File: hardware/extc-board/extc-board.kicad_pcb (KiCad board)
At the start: 2 copper layers, 38.5 x 85 mm, 19 parts, among them J1 GH BM07B link to INT, J2 VCC DATA GND, J3 PTSM 0,5/2-HH-2,5-SMD 24 VAC, J4 PTSM 0,5/2-HV-2,5-SMD 5V OUT, U1 DS2482-100, U3 TMR 12-4811WI

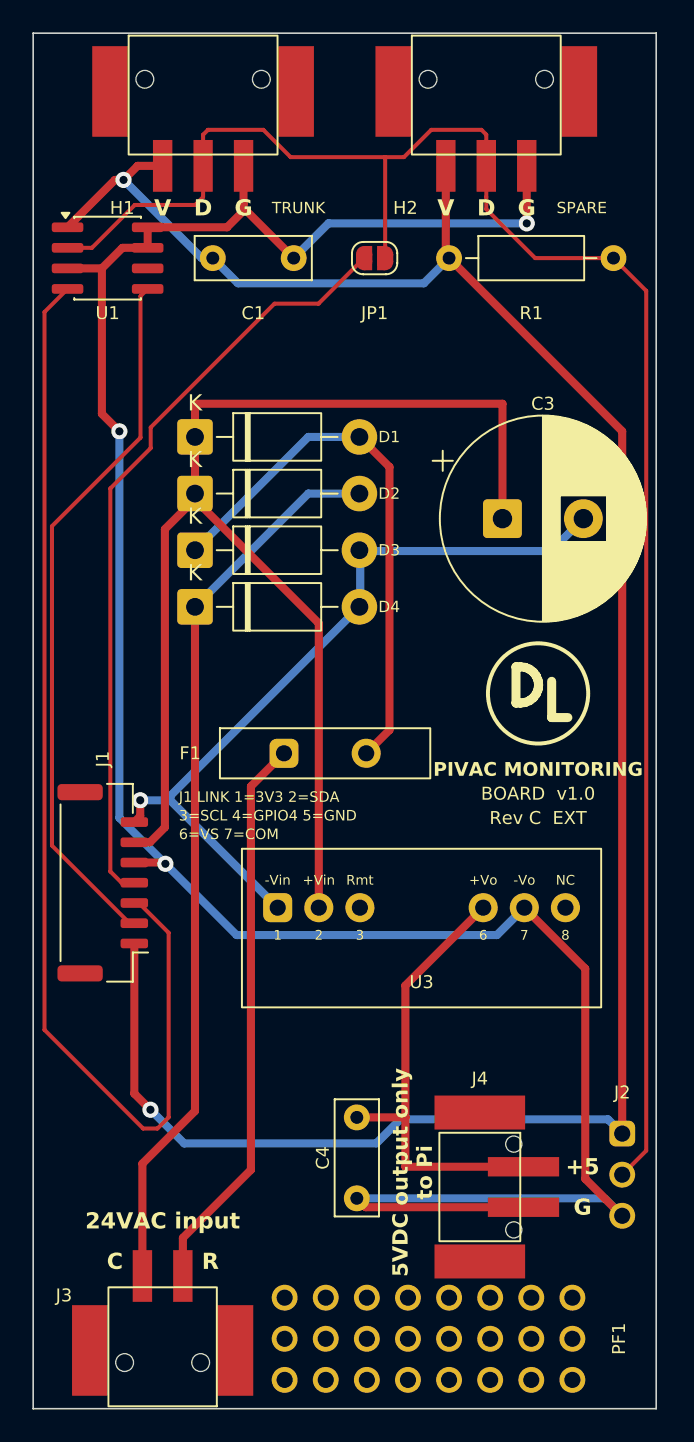
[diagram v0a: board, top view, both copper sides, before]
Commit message: Rev C: no copper under U3 but its pin escapes, no via under a legend, J1 label clear
Traco's datasheet says to avoid routing traces under the converter, whose
case is copper. The first routed board had 65 mm of track under it. Rule
areas now close the component side under the whole body and the solder
side except a 2 mm channel from each connected pin to the nearer edge,
3.5 mm away. The pins stand inside the outline, so those four escapes are
the least copper that can reach them.

The router then took the Pi's 5 V round the converter's left end, 62 mm
at 0.5 mm. It is laid by hand instead on the solder side at 1.0 mm round
the right end: 47 and 55 mm, about 25 mohm each.

Rule areas over each legend keep vias out from under the letters, which
removes the via under H2's G. The J1 reference reads left to right above
the header, clear of its mounting pad.

Co-Authored-By: Claude Fable 5.1 <noreply@anthropic.com>
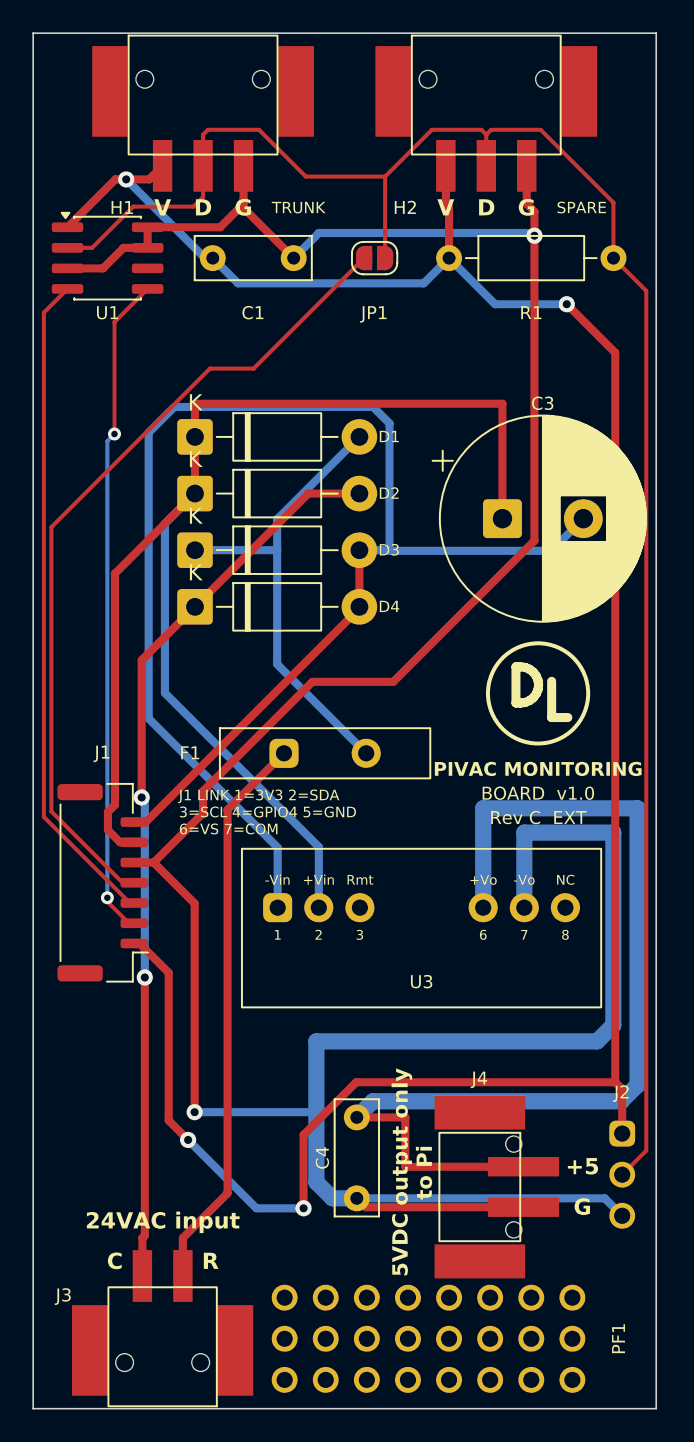
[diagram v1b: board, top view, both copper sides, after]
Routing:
- net COM: track 47.7 -> 94.1 mm, vias 1 -> 0
- net GND: track 153.0 -> 196.7 mm, vias 3 -> 2
- net +5V: track 28.3 -> 64.3 mm
- net SCL: track 71.2 -> 41.0 mm
- net VCC: track 136.9 -> 145.3 mm, vias 2 -> 4
- net ACF: track 34.0 -> 29.0 mm
- net VS: track 83.7 -> 86.9 mm
- net GPIO4: track 47.8 -> 50.7 mm
- net SDA: track 43.9 -> 41.1 mm, vias 0 -> 2
- net DATA: track 110.7 -> 112.0 mm
- net ACC: track 55.8 -> 55.9 mm, vias 0 -> 2

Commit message: Rev C: socket labels beside their connectors, U3's reference outside its outline
H1, H2, TRUNK and SPARE sat on the row of pin letters, one row from the
sockets they name. They move up beside each socket's leads. U3's
reference sat inside the outline, under the converter; it moves below it.
Rule areas keep vias out from under the moved labels and the row of
references under the sockets.

Co-Authored-By: Claude Fable 5.1 <noreply@anthropic.com>
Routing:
- net COM: track 94.1 -> 48.6 mm, vias 0 -> 1
- net SCL: track 41.0 -> 50.3 mm
- net GND: track 196.7 -> 188.1 mm, vias 2 -> 4
- net VCC: track 145.3 -> 152.9 mm, vias 4 -> 3
- net SDA: track 41.1 -> 44.3 mm, vias 2 -> 0
- net GPIO4: track 50.7 -> 47.7 mm
- net VS: track 86.9 -> 84.0 mm
- net ACC: track 55.9 -> 55.8 mm, vias 2 -> 0

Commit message: Rev C: U3's pin names on the solder side too
The names on the component side are under the converter once it is
fitted. The solder side is where the meter goes after soldering.

Co-Authored-By: Claude Fable 5.1 <noreply@anthropic.com>
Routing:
- net DATA: track 112.0 -> 136.4 mm, vias 0 -> 1
- net GPIO4: track 47.7 -> 66.8 mm
- net COM: track 48.6 -> 62.8 mm, vias 1 -> 0
- net SCL: track 50.3 -> 40.6 mm
- net VCC: track 152.9 -> 144.0 mm, vias 3 -> 2
- net VS: track 84.0 -> 92.0 mm
- net GND: track 188.1 -> 189.8 mm, vias 4 -> 5
- net SDA: track 44.3 -> 42.6 mm, vias 0 -> 2
- net ACC: vias 0 -> 1
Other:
- board text added: "+Vin"
- board text added: "+Vo"
- board text added: "-Vin"
- board text added: "-Vo"
- board text added: "1"
- board text added: "2"
- board text added: "3"
- board text added: "6"
- board text added: "7"
- board text added: "8"
- board text added: "NC"
- board text added: "Rmt"
- board text added: "U3"

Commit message: Rev C: fit check against Phoenix's STEP models; anchor pads moved 0.4 mm (#219)
* Rev C: fit check against Phoenix's STEP models; anchor pads moved 0.4 mm

hardware/fit-check.py lays the STEP models on the footprints of the
generated board and reports the margin of every solder foot inside its
pad and the play of every peg in its hole. It replaces the check in
KiCad's 3D viewer, and stands in for laying a header on a print until
the headers arrive.

Its first run found the horizontal header's anchor feet 0.1 mm off the
rear of their pads. The pads were placed 0.8 to 6.4 mm from the face; the
feet lie 1.5 to 6.5 mm from it. Phoenix's drawing puts the pad's end
0.2 mm past the start of the signal pads, which I had read as 0.2 mm
short of it. The pads are now 1.2 to 6.8 mm from the face, centred on
the feet with 0.3 mm to spare at each end.

The three STEP models are in hardware/vendor with the housing models.

Co-Authored-By: Claude Fable 5.1 <noreply@anthropic.com>

* Rev C: fit check against the models of the parts being fitted; H1 and H2 are HH0

David supplied the models of the three connectors he is fitting. The
check now lays each on its own footprint: 1808200 on H1 and H2, 1778764
on J3, 1778696 on J4. Every foot lies on its pad and every peg in its
hole.

1808200 is the HH0 header, the HH without its two locating pegs; body,
anchors, leads and latch windows are the same. The footprint keeps its
peg holes, which stay empty under an HH0, so the board takes either.

The board's copper and gerbers are unchanged: only the value of H1 and
H2 in the board, schematic and BOM. DRC is still clean.

The housing check is closed: David confirms a plug seats with the header
faces on the board edge.

Co-Authored-By: Claude Fable 5.1 <noreply@anthropic.com>

---------

Co-authored-by: Claude Fable 5.1 <noreply@anthropic.com>
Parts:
- H1, H2: value PTSM 0,5/3-HH-2,5-SMD -> PTSM 0,5/3-HH0-2,5-SMD
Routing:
- net COM: track 62.8 -> 48.2 mm, vias 0 -> 1
- net DATA: track 136.4 -> 124.9 mm, vias 1 -> 0
- net GPIO4: track 66.8 -> 55.5 mm
- net VCC: track 144.0 -> 150.6 mm, vias 2 -> 3
- net VS: track 92.0 -> 85.6 mm, vias 0 -> 1
- net SDA: track 42.6 -> 41.0 mm, vias 2 -> 0
- net GND: track 189.8 -> 189.2 mm, vias 5 -> 4
- net ACC: vias 1 -> 0

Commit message: Rev C: H1 and H2 are 1778777, the 3-way header with locating pegs
David swapped the order from the HH0 header to the HH. Only the part's
value changes in the board, schematic and BOM; copper and gerbers are
as they were.

Co-Authored-By: Claude Fable 5.1 <noreply@anthropic.com>
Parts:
- H1, H2: value PTSM 0,5/3-HH0-2,5-SMD -> PTSM 0,5/3-HH-2,5-SMD
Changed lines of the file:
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@@
 		(layer "F.Cu")
 		(at 28 0)
-		(descr "Phoenix Contact PTSM 0,5/3-HH0-2,5-SMD horizontal header, surface mount")
+		(descr "Phoenix Contact PTSM 0,5/3-HH-2,5-SMD horizontal header, surface mount")
 		(property "Reference" "H2"
 			(at -5.3 8.199999 0)
@@
 			)
 		)
-		(property "Value" "PTSM 0,5/3-HH0-2,5-SMD"
+		(property "Value" "PTSM 0,5/3-HH-2,5-SMD"
 			(at 0 12.2 0)
 			(layer "F.Fab")
@@
 		(layer "F.Cu")
 		(at 10.5 0)
-		(descr "Phoenix Contact PTSM 0,5/3-HH0-2,5-SMD horizontal header, surface mount")
+		(descr "Phoenix Contact PTSM 0,5/3-HH-2,5-SMD horizontal header, surface mount")
 		(property "Reference" "H1"
 			(at -5.3 8.199999 0)
@@
 			)
 		)
-		(property "Value" "PTSM 0,5/3-HH0-2,5-SMD"
+		(property "Value" "PTSM 0,5/3-HH-2,5-SMD"
 			(at 0 12.2 0)
 			(layer "F.Fab")

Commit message: Rev C: fit check against the models of the parts being fitted; H1 and H2 are HH0
David supplied the models of the three connectors he is fitting. The
check now lays each on its own footprint: 1808200 on H1 and H2, 1778764
on J3, 1778696 on J4. Every foot lies on its pad and every peg in its
hole.

1808200 is the HH0 header, the HH without its two locating pegs; body,
anchors, leads and latch windows are the same. The footprint keeps its
peg holes, which stay empty under an HH0, so the board takes either.

The board's copper and gerbers are unchanged: only the value of H1 and
H2 in the board, schematic and BOM. DRC is still clean.

The housing check is closed: David confirms a plug seats with the header
faces on the board edge.

Co-Authored-By: Claude Fable 5.1 <noreply@anthropic.com>
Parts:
- H1, H2: value PTSM 0,5/3-HH-2,5-SMD -> PTSM 0,5/3-HH0-2,5-SMD
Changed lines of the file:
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@@
 		(layer "F.Cu")
 		(at 28 0)
-		(descr "Phoenix Contact PTSM 0,5/3-HH-2,5-SMD horizontal header, surface mount")
+		(descr "Phoenix Contact PTSM 0,5/3-HH0-2,5-SMD horizontal header, surface mount")
 		(property "Reference" "H2"
 			(at -5.3 8.199999 0)
@@
 			)
 		)
-		(property "Value" "PTSM 0,5/3-HH-2,5-SMD"
+		(property "Value" "PTSM 0,5/3-HH0-2,5-SMD"
 			(at 0 12.2 0)
 			(layer "F.Fab")
@@
 		(layer "F.Cu")
 		(at 10.5 0)
-		(descr "Phoenix Contact PTSM 0,5/3-HH-2,5-SMD horizontal header, surface mount")
+		(descr "Phoenix Contact PTSM 0,5/3-HH0-2,5-SMD horizontal header, surface mount")
 		(property "Reference" "H1"
 			(at -5.3 8.199999 0)
@@
 			)
 		)
-		(property "Value" "PTSM 0,5/3-HH-2,5-SMD"
+		(property "Value" "PTSM 0,5/3-HH0-2,5-SMD"
 			(at 0 12.2 0)
 			(layer "F.Fab")
